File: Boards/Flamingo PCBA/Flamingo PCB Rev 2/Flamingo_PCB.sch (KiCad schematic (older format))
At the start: 4 parts

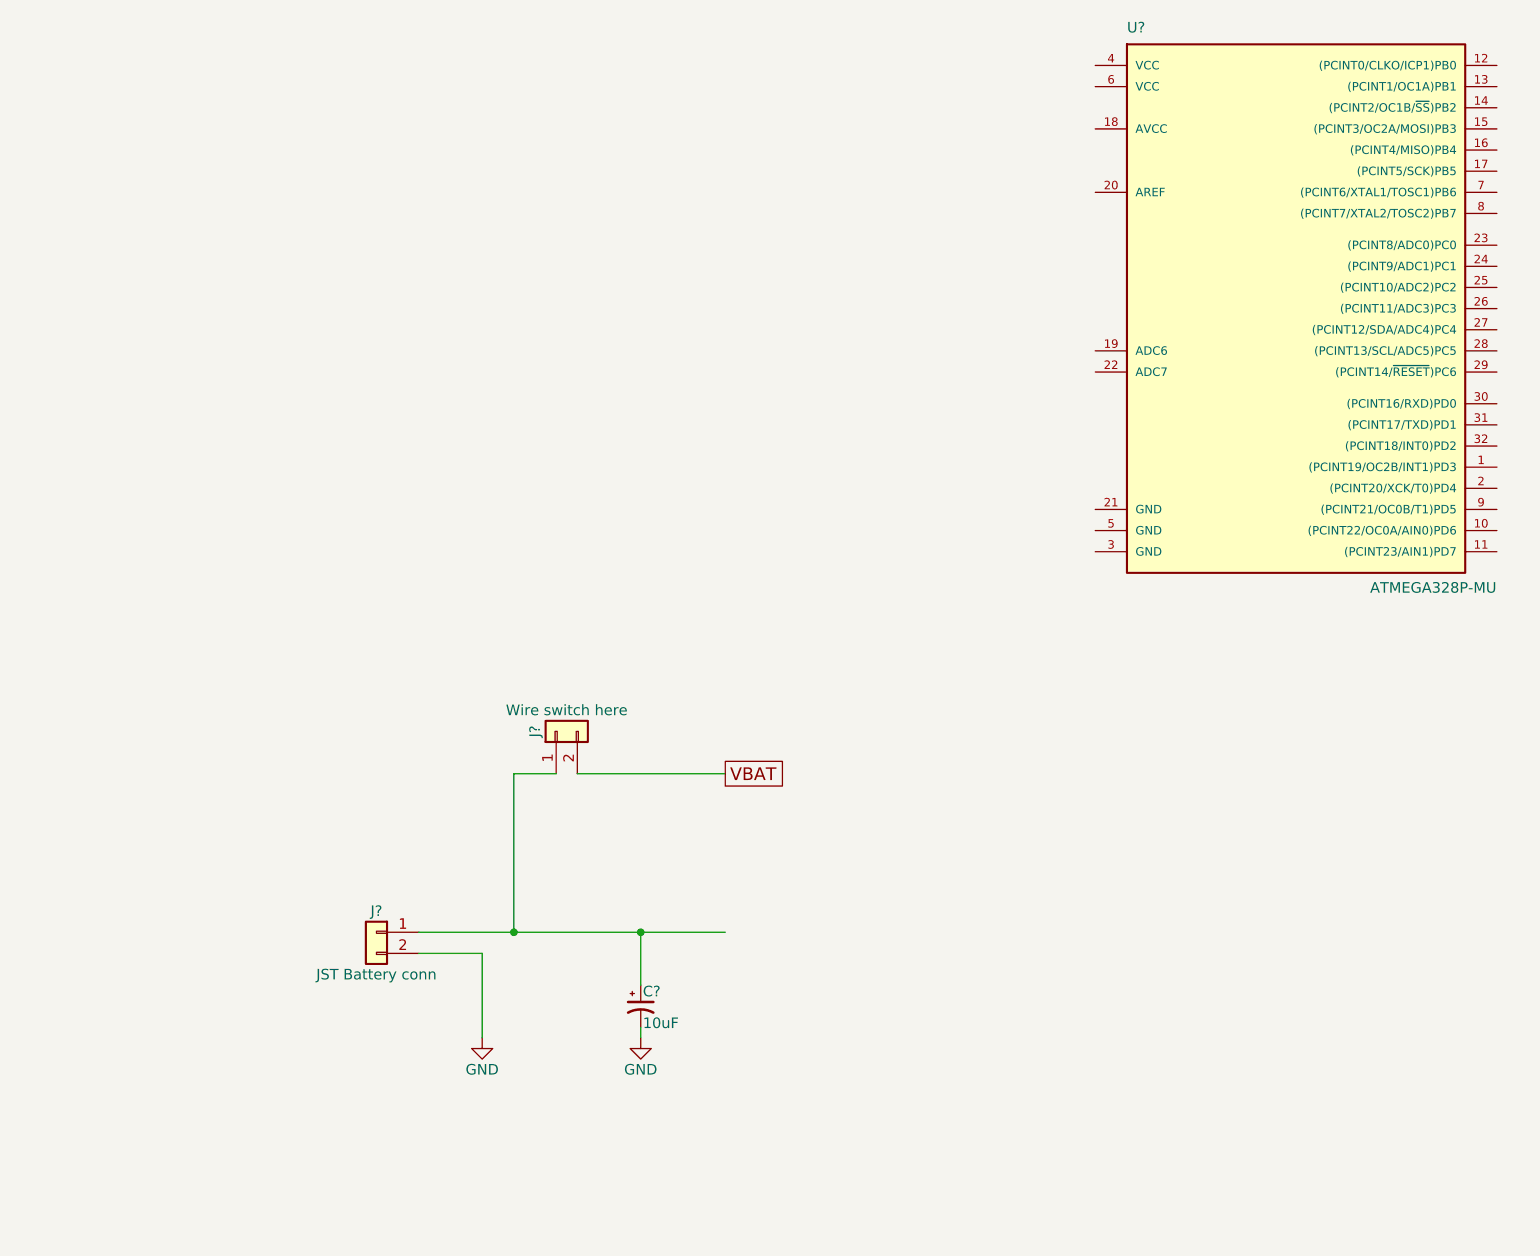
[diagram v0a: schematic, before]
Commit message: First pass of battery charging section complete
Still needs another pass for component and value selection.
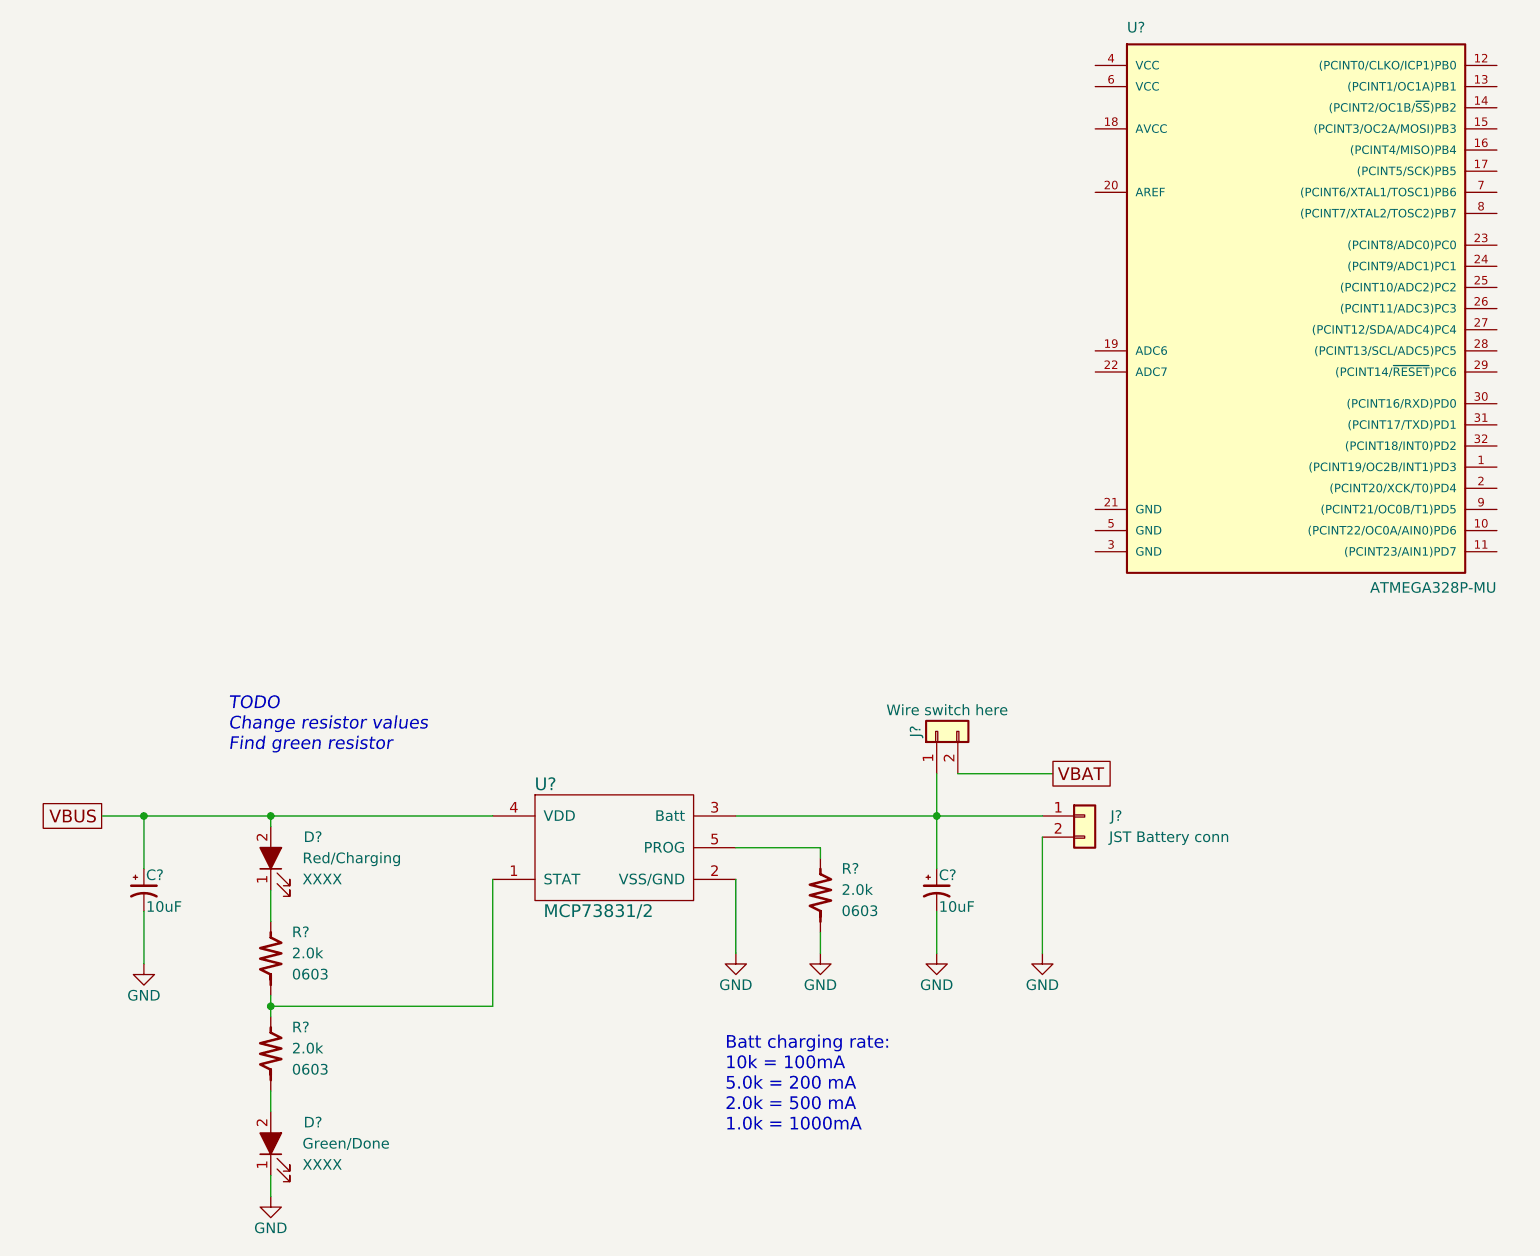
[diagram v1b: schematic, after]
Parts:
- added C?: 10uF, symbol CP1_Small
- added D?: Red/Charging, symbol LED_ALT_vert
- added D?: Green/Done, symbol LED_ALT_vert
- added R? (x3): 2.0k, symbol R_vert
- added U?: MCP73831/2, symbol MCP73831/2
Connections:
- net labels added: VBUS
- wire segments 8 -> 24
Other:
- note added: "Batt charging rate:\n10k = 100mA\n5.0k = 200 mA\n2.0k = 500 mA\n1.0k = 1000mA"
- note added: "TODO\nChange resistor values\nFind green resistor"
- moved on the sheet: C?, J?
